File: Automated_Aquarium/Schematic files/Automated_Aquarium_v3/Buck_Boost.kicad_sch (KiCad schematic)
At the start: 15 parts, among them U3 TPS631000DRLR

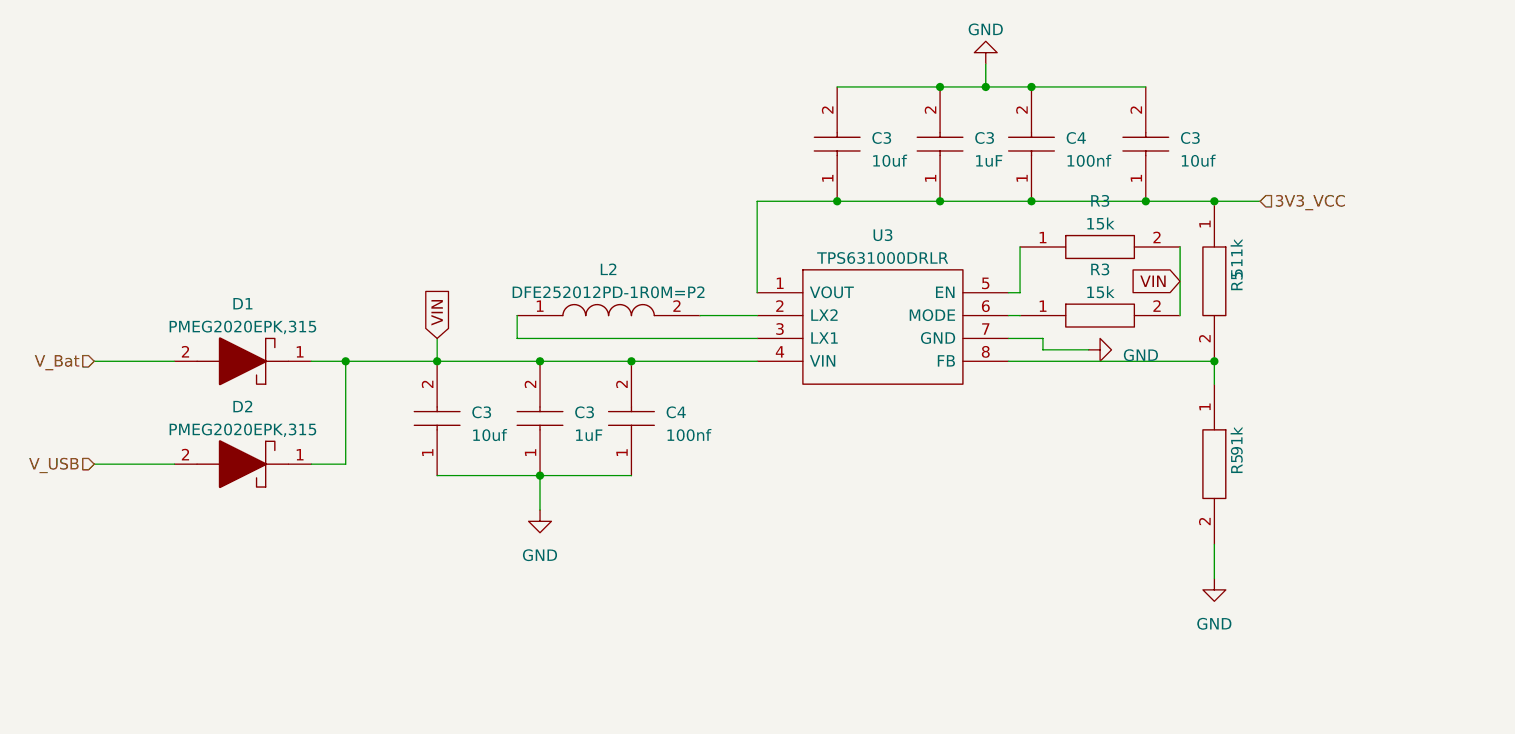
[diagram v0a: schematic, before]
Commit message: complete 0v1 layout aquarium
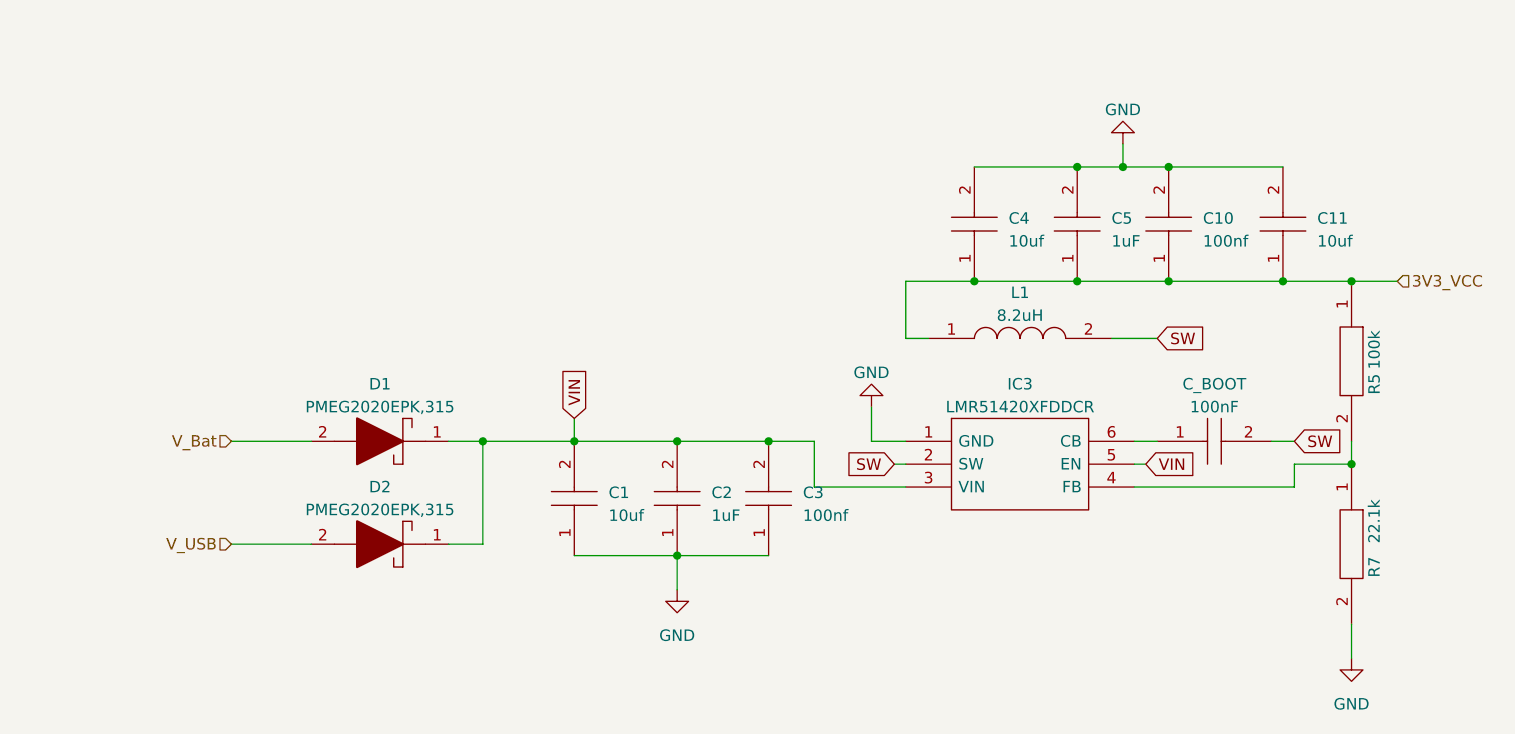
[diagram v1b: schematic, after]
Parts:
- removed C3 (x3): 10uf, Capacitor_SMD:C_0603_1608Metric_Pad1.08x0.95mm_HandSolder, symbol SamacSys_Parts:0402B102K500NT
- removed C3 (x2): 1uF, Capacitor_SMD:C_0603_1608Metric_Pad1.08x0.95mm_HandSolder, symbol SamacSys_Parts:0402B102K500NT
- removed C4 (x2): 100nf, Capacitor_SMD:C_0603_1608Metric_Pad1.08x0.95mm_HandSolder, symbol SamacSys_Parts:0402B102K500NT
- removed L2: DFE252012PD-1R0M=P2, DFE2HCAH1R0MJ0L, symbol SamacSys_Parts:DFE252012PD-1R0M=P2
- removed R3 (x2): 15k, RESC1608X55N, symbol SamacSys_Parts:RMCF0603ZT0R00
- removed R5: 91k, RESC1608X55N, symbol SamacSys_Parts:RMCF0603ZT0R00
- removed R5: 511k, RESC1608X55N, symbol SamacSys_Parts:RMCF0603ZT0R00
- removed U3: TPS631000DRLR, SOTFL50P160X60-8N, symbol SamacSys_Parts:TPS631000DRLR
- added C1, C11, C4: 10uf, Capacitor_SMD:C_0603_1608Metric_Pad1.08x0.95mm_HandSolder, symbol SamacSys_Parts:0402B102K500NT
- added C10, C3: 100nf, Capacitor_SMD:C_0603_1608Metric_Pad1.08x0.95mm_HandSolder, symbol SamacSys_Parts:0402B102K500NT
- added C2, C5: 1uF, Capacitor_SMD:C_0603_1608Metric_Pad1.08x0.95mm_HandSolder, symbol SamacSys_Parts:0402B102K500NT
- added C_BOOT: 100nF, Capacitor_SMD:C_0603_1608Metric_Pad1.08x0.95mm_HandSolder, symbol SamacSys_Parts:0402B102K500NT
- added IC3: LMR51420XFDDCR, SOT95P280X110-6N, symbol SamacSys_Parts:LMR51420XFDDCR
- added L1: 8.2uH, DFE2HCAH1R0MJ0L, symbol SamacSys_Parts:DFE252012PD-1R0M=P2
- added R5: 100k, RESC1608X55N, symbol SamacSys_Parts:RMCF0603ZT0R00
- added R7: 22.1k, RESC1608X55N, symbol SamacSys_Parts:RMCF0603ZT0R00
- D1, D2: LCSC Part Number (none) -> C552841; MPN (none) -> C552841
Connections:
- net 3V3_VCC: now also C10.1, C11.1, C4.1, C5.1, L1.1, R5.1
- net GND: now also C1.1, C10.2, C11.2, C2.1, C3.1, C4.2, C5.2, IC3.1 (GND), R7.2
- net VIN: now also C1.2, C2.2, C3.2, IC3.3 (VIN), IC3.5 (EN)
- new net: IC3.4 (FB), R5.2, R7.1
- new net: C_BOOT.1, IC3.6 (CB)
- new net SW: C_BOOT.2, IC3.2 (SW), L1.2

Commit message: init pcb
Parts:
- renumbered C_BOOT to C_BOOT1
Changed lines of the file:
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@@
   (symbol (lib_id "SamacSys_Parts:0402B102K500NT") (at 186.69 83.82 0) (unit 1)
     (in_bom yes) (on_board yes) (dnp no) (fields_autoplaced)
-    (property "Reference" "C_BOOT" (at 193.04 77.47 0)
+    (property "Reference" "C_BOOT1" (at 193.04 77.47 0)
       (effects (font (size 1.27 1.27)))
     )
@@
       (project "Automated_Aquarium_v3"
         (path "/953ef1f2-1b30-471f-8352-2e2b084ebc55/74cfcaf9-5269-4ba4-8d15-75996e6dd2a1"
-          (reference "C_BOOT") (unit 1)
+          (reference "C_BOOT1") (unit 1)
         )
       )

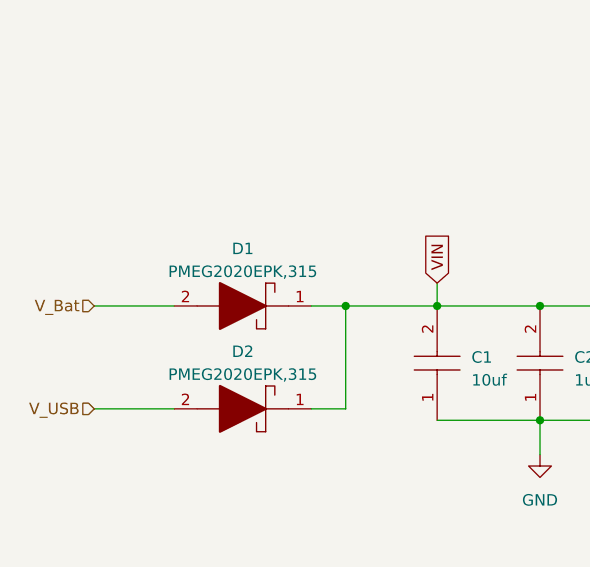
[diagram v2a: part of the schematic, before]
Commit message: finish aqua schem, add inital layout
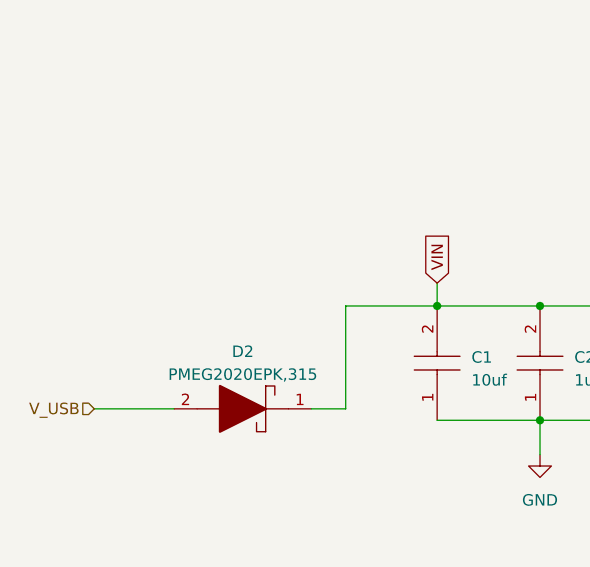
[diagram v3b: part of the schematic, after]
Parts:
- removed D1: PMEG2020EPK,315, PMEG2020EPK315, symbol SamacSys_Parts:PMEG2020EPK,315
- C10, C3: LCSC Part Number C14663 -> C307349
- C2, C5: LCSC Part Number C15849 -> C377755
- C_BOOT1: LCSC Part Number C96446 -> C307349
- IC3: LCSC Part Number (none) -> C5383002
- R5: LCSC Part Number C3016414 -> C855633
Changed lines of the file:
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@@
   (junction (at 133.35 96.52) (diameter 0) (color 0 0 0 0)
   )
-  (junction (at 111.76 83.82) (diameter 0) (color 0 0 0 0)
-  )
   (junction (at 208.28 66.04) (diameter 0) (color 0 0 0 0)
   )
@@
     (stroke (width 0) (type default))
   )
-  (wire (pts (xy 107.95 83.82) (xy 111.76 83.82))
-    (stroke (width 0) (type default))
-  )
   (wire (pts (xy 181.61 72.39) (xy 186.69 72.39))
     (stroke (width 0) (type default))
@@
   )
   (wire (pts (xy 111.76 83.82) (xy 121.92 83.82))
-    (stroke (width 0) (type default))
-  )
-  (wire (pts (xy 83.82 83.82) (xy 92.71 83.82))
     (stroke (width 0) (type default))
   )
@@
     (effects (font (size 1.27 1.27)) (justify left))
   )
-  (hierarchical_label "V_Bat" (shape input) (at 83.82 83.82 180) (fields_autoplaced)
-    (effects (font (size 1.27 1.27)) (justify right))
-    (property "Intersheetrefs" "${INTERSHEET_REFS}" (at 75.7133 83.82 0)
-      (effects (font (size 1.27 1.27)) (justify right) hide)
-    )
-  )
   (symbol (lib_id "SamacSys_Parts:LMR51420XFDDCR") (at 158.75 83.82 0) (unit 1)
     (in_bom yes) (on_board yes) (dnp no) (fields_autoplaced)
@@
     (property "Arrow Price/Stock" "https://www.arrow.com/en/products/lmr51420xfddcr/texas-instruments?region=nac" (at 180.34 104.14 0)
       (effects (font (size 1.27 1.27)) (justify left) hide)
+    )
+    (property "LCSC Part Number" "C5383002" (at 158.75 83.82 0)
+      (effects (font (size 1.27 1.27)) hide)
     )
     (pin "1")
@@
       (effects (font (size 1.27 1.27)) hide)
     )
-    (property "LCSC Part Number" "C15849" (at 177.8 66.04 0)
+    (property "LCSC Part Number" "C377755" (at 177.8 66.04 0)
       (effects (font (size 1.27 1.27)) hide)
     )
@@
       (effects (font (size 1.27 1.27)) hide)
     )
-    (property "LCSC Part Number" "C15849" (at 133.35 96.52 0)
+    (property "LCSC Part Number" "C377755" (at 133.35 96.52 0)
       (effects (font (size 1.27 1.27)) hide)
     )
@@
       (effects (font (size 1.27 1.27)) (justify left) hide)
     )
-    (property "LCSC Part Number" "C14663" (at 187.96 66.04 0)
+    (property "LCSC Part Number" "C307349" (at 187.96 66.04 0)
       (effects (font (size 1.27 1.27)) hide)
     )
@@
       (effects (font (size 1.27 1.27)) (justify left) hide)
     )
-    (property "LCSC Part Number" "C3016414" (at 208.28 66.04 0)
+    (property "LCSC Part Number" "C855633" (at 208.28 66.04 0)
       (effects (font (size 1.27 1.27)) hide)
     )
@@
     )
   )
-  (symbol (lib_id "SamacSys_Parts:PMEG2020EPK,315") (at 110.49 83.82 180) (unit 1)
-    (in_bom yes) (on_board yes) (dnp no) (fields_autoplaced)
-    (property "Reference" "D1" (at 100.33 77.47 0)
-      (effects (font (size 1.27 1.27)))
-    )
-    (property "Value" "PMEG2020EPK,315" (at 100.33 80.01 0)
-      (effects (font (size 1.27 1.27)))
-    )
-    (property "Footprint" "PMEG2020EPK315" (at 97.79 87.63 0)
-      (effects (font (size 1.27 1.27)) (justify left) hide)
-    )
-    (property "Datasheet" "https://assets.nexperia.com/documents/data-sheet/PMEG2020EPK.pdf" (at 97.79 85.09 0)
-      (effects (font (size 1.27 1.27)) (justify left) hide)
-    )
-    (property "Description" "NEXPERIA - PMEG2020EPK,315 - Schottky Rectifier, 20 V, 2 A, Single, SOD-1608, 2 Pins, 450 mV" (at 97.79 82.55 0)
-      (effects (font (size 1.27 1.27)) (justify left) hide)
-    )
-    (property "Height" "0.4" (at 97.79 80.01 0)
-      (effects (font (size 1.27 1.27)) (justify left) hide)
-    )
-    (property "Manufacturer_Name" "Nexperia" (at 97.79 77.47 0)
-      (effects (font (size 1.27 1.27)) (justify left) hide)
-    )
-    (property "Manufacturer_Part_Number" "PMEG2020EPK,315" (at 97.79 74.93 0)
-      (effects (font (size 1.27 1.27)) (justify left) hide)
-    )
-    (property "Mouser Part Number" "771-PMEG2020EPK,315" (at 97.79 72.39 0)
-      (effects (font (size 1.27 1.27)) (justify left) hide)
-    )
-    (property "Mouser Price/Stock" "https://www.mouser.co.uk/ProductDetail/Nexperia/PMEG2020EPK315?qs=zHGtguZFFhKxs4HM5hK1uw%3D%3D" (at 97.79 69.85 0)
-      (effects (font (size 1.27 1.27)) (justify left) hide)
-    )
-    (property "Arrow Part Number" "PMEG2020EPK,315" (at 97.79 67.31 0)
-      (effects (font (size 1.27 1.27)) (justify left) hide)
-    )
-    (property "Arrow Price/Stock" "https://www.arrow.com/en/products/pmeg2020epk315/nexperia?region=nac" (at 97.79 64.77 0)
-      (effects (font (size 1.27 1.27)) (justify left) hide)
-    )
-    (property "Digi-Key_PN" "771-PMEG2020EPK,315" (at 110.49 83.82 0)
-      (effects (font (size 1.27 1.27)) hide)
-    )
-    (property "LCSC Part Number" "C552841" (at 110.49 83.82 0)
-      (effects (font (size 1.27 1.27)) hide)
-    )
-    (property "MPN" "C552841" (at 110.49 83.82 0)
-      (effects (font (size 1.27 1.27)) hide)
-    )
-    (pin "1")
-    (pin "2")
-    (instances
-      (project "Automated_Aquarium_v3"
-        (path "/953ef1f2-1b30-471f-8352-2e2b084ebc55/74cfcaf9-5269-4ba4-8d15-75996e6dd2a1"
-          (reference "D1") (unit 1)
-        )
-      )
-      (project "Dot-LED"
-        (path "/e63e39d7-6ac0-4ffd-8aa3-1841a4541b55/eadb16b8-295e-4810-8d56-9eb69942c69b"
-          (reference "D1") (unit 1)
-        )
-      )
-    )
-  )
   (symbol (lib_id "SamacSys_Parts:0402B102K500NT") (at 121.92 96.52 90) (unit 1)
     (in_bom yes) (on_board yes) (dnp no) (fields_autoplaced)
@@
       (effects (font (size 1.27 1.27)) hide)
     )
-    (property "LCSC Part Number" "C96446" (at 186.69 83.82 0)
+    (property "LCSC Part Number" "C307349" (at 186.69 83.82 0)
       (effects (font (size 1.27 1.27)) hide)
     )
@@
       (effects (font (size 1.27 1.27)) (justify left) hide)
     )
-    (property "LCSC Part Number" "C14663" (at 143.51 96.52 0)
-      (effects (font (size 1.27 1.27)) hide)
-    )
+    (property "LCSC Part Number" "C307349" (at 143.51 96.52 0)
+      (effects (font (size 1.27 1.27)) hide)
+    )
